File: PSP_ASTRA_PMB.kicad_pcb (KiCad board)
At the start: 2 copper layers, 15 parts, among them J1 Conn_01x02_Socket, J2 Conn_01x01_Socket, J3 Screw_Terminal_01x03, J5 Screw_Terminal_01x01, J6 Screw_Terminal_01x01, Q1 BSC014N04LSIATMA1, U1 INA226, U5 LD1117V33

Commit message: Add files via upload
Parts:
- moved J6 42.8 mm to (151.0, 110.0)
- moved J5 33.3 mm to (150.0, 84.5)
- moved U5 23.6 mm to (145.4, 93.5)
- moved C3 18.4 mm to (154.0, 97.5), turned to 180 degrees
- moved R2 18.3 mm to (143.5, 105.0)
- moved C2 15.5 mm to (148.5, 97.5)
- moved C1 15.5 mm to (143.5, 98.0), turned to 180 degrees
- moved J1 14.7 mm to (138.5, 101.4), turned to -90 degrees
- moved Q1 13.2 mm to (170.5, 110.0)
- moved R3 11.9 mm to (143.5, 101.5)
- moved J3 9.50 mm to (133.0, 94.0), turned to 90 degrees
- moved R4 5.03 mm to (165.0, 89.0)
- moved J2 3.16 mm to (156.0, 103.5)
- moved U1 2.06 mm to (150.5, 102.0)
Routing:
- net /Microcontroller: track 0.00 -> 0.85 mm
- added copper zone on B.Cu, net GND
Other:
- copper layers 2 -> 4

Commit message: Add files via upload
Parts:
- Q1: footprint Package_TO_SOT_SMD:TDSON-8-1 -> PSPAC:MOSFETPMB
- R1, R2, R3: footprint Resistor_SMD:R_0805_2012Metric -> Resistor_SMD:R_0805_2012Metric_Pad1.20x1.40mm_HandSolder
- moved R1 21.9 mm to (156.0, 100.5)
- moved Q1 8.49 mm to (162.5, 107.3), turned to -90 degrees
- moved J1 6.08 mm to (144.0, 104.0)
- moved R2 5.25 mm to (143.5, 110.2)
- moved R4 3.15 mm to (168.0, 90.0)
- moved C3 1.00 mm to (155.0, 97.5)
- moved J2 0.71 mm to (155.5, 104.0)
- moved U1 0.50 mm to (150.0, 102.0)
- moved U5 0.30 mm to (145.5, 93.2)
- moved J6 0.25 mm to (150.8, 110.0)
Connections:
- net Net-(Q1-D) renamed /Drain
- J6 pad 1: Net-(J6-Pin_1) -> /Source
- Q1 pad 4: (no net) -> /Microcontroller
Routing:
- net +12V: track 0.00 -> 33.7 mm, vias 0 -> 7
- net Net-(U1-VS): track 0.00 -> 32.0 mm
- net GND: track 0.00 -> 11.8 mm, vias 0 -> 6
- net /Drain: track 0.00 -> 11.4 mm, vias 0 -> 7
- net Net-(J1-Pin_2): track 0.00 -> 10.9 mm
- net /Microcontroller: track 0.85 -> 8.91 mm
- net Net-(J1-Pin_1): track 0.00 -> 6.84 mm
- net /Source: vias 0 -> 6
- added copper zone on B.Cu, net +12V
- added copper zone on F.Cu, net +12V
- added copper zone on In1.Cu, net +12V
- added copper zone on In2.Cu, net +12V
- added copper zone on B.Cu, net /Drain
- added copper zone on F.Cu, net /Drain
- added copper zone on In1.Cu, net /Drain
- added copper zone on In2.Cu, net /Drain
- added copper zone on B.Cu, net /Source
- added copper zone on F.Cu, net /Source
- added copper zone on In1.Cu, net /Source
- added copper zone on In2.Cu, net /Source
- added copper zone on In1.Cu, net GND
- removed copper zone on B.Cu, net GND
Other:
- board outline added: 47 x 36 mm

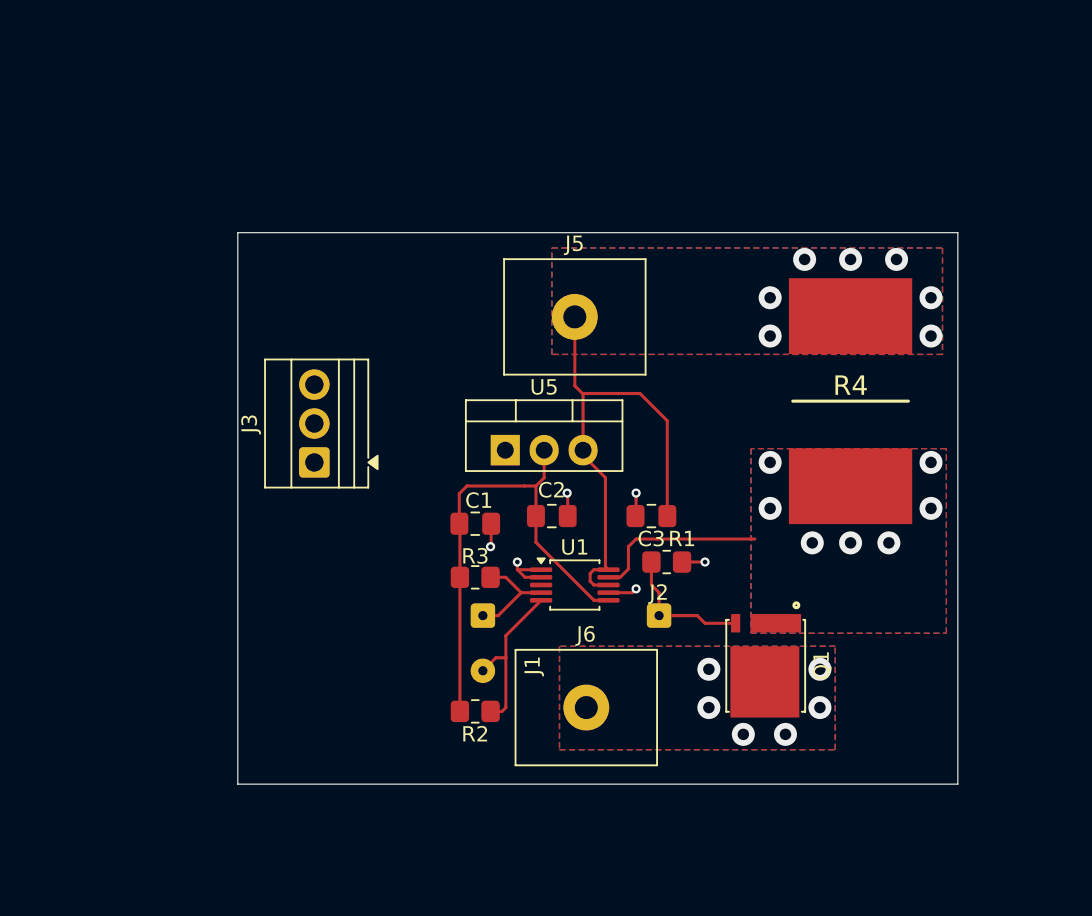
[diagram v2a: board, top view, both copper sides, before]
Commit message: Add files via upload
added pmos and voltage divider (see schematic)
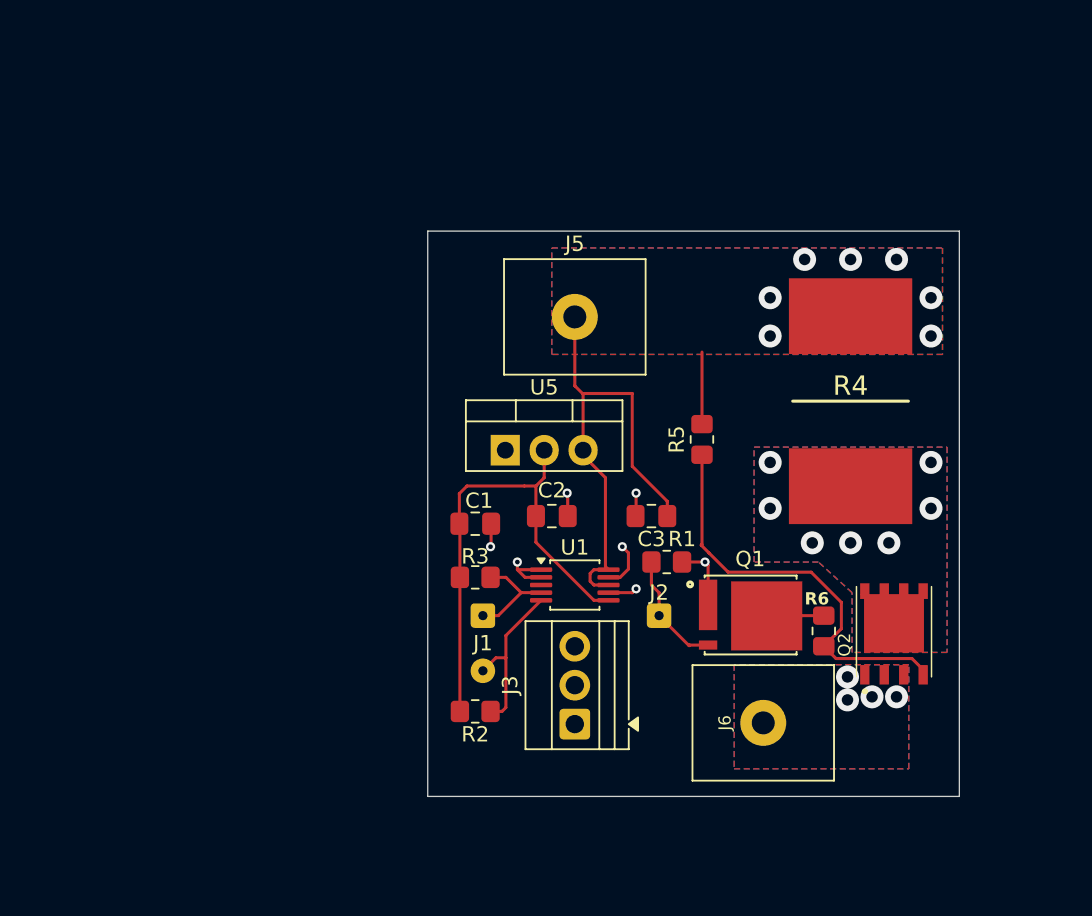
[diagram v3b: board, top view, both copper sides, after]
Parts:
- added Q2: PMOS, PSPAC:PMOSPMB, F.Cu at (170.8, 105.0)
- added R5: 10k, Resistor_SMD:R_0805_2012Metric_Pad1.20x1.40mm_HandSolder, F.Cu at (158.3, 92.5)
- added R6: 10, Resistor_SMD:R_0805_2012Metric_Pad1.20x1.40mm_HandSolder, F.Cu at (166.2, 105.0)
- moved J3 24.1 mm to (150.0, 111.1)
- moved J6 11.6 mm to (162.3, 111.0)
- moved Q1 3.46 mm to (161.5, 104.0), turned to 0 degrees
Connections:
- J6 pad 1: /Source -> /PMOS Source
- Q1 pad 1: /Drain -> GND
- Q1 pad 8: /Source -> /NMOS Drain
- R4 pad 2: /Drain -> /PMOS Drain
- U1 pad 9: /Drain -> /PMOS Drain
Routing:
- net /PMOS Gate: track 0.00 -> 27.4 mm
- net /PMOS Drain: track 0.00 -> 13.8 mm, vias 0 -> 8
- net /Drain: track 11.4 -> 0.00 mm, vias 7 -> 0
- net /NMOS Drain: track 0.00 -> 4.76 mm
- net +12V: track 33.7 -> 38.2 mm
- net GND: track 11.8 -> 14.6 mm
- net /Microcontroller: track 8.91 -> 7.74 mm
- net /PMOS Source: track 0.00 -> 0.33 mm, vias 0 -> 4
- net /Source: vias 6 -> 0
- added copper zone on B.Cu, net /PMOS Drain
- added copper zone on F.Cu, net /PMOS Drain
- added copper zone on In1.Cu, net /PMOS Drain
- added copper zone on In2.Cu, net /PMOS Drain
- added copper zone on B.Cu, net /PMOS Source
- added copper zone on F.Cu, net /PMOS Source
- added copper zone on In1.Cu, net /PMOS Source
- added copper zone on In2.Cu, net /PMOS Source
- removed copper zone on B.Cu, net /Drain
- removed copper zone on F.Cu, net /Drain
- removed copper zone on In1.Cu, net /Drain
- removed copper zone on In2.Cu, net /Drain
- removed copper zone on B.Cu, net /Source
- removed copper zone on F.Cu, net /Source
- removed copper zone on In1.Cu, net /Source
- removed copper zone on In2.Cu, net /Source
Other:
- board size 47 x 36 mm -> 34.7 x 36.9 mm

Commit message: Add files via upload
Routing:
- net /PMOS Drain: track 13.8 -> 12.1 mm
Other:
- board text added: "${REFERENCE}"
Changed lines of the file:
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@@
 		(tags "THT Terminal Block Xinya XY308-2.54-3P pitch 2.54mm size 8.12x6.5mm drill 1.2mm pad 2mm")
 		(property "Reference" "J3"
-			(at 2.54 -4.22 90)
+			(at -2.47 -0.05 180)
 			(layer "F.SilkS")
 			(effects
@@
 		(tags "capacitor handsolder")
 		(property "Reference" "C3"
-			(at 0 -1.5 0)
+			(at -1.9 1.65 0)
 			(layer "F.SilkS")
 			(effects
@@
 		(at 161.475 103.96)
 		(property "Reference" "Q1"
-			(at -0.02513 -3.65372 0)
+			(at -0.625 -3.56 0)
 			(layer "F.SilkS")
 			(effects
@@
 		(tags "THT single screw terminal block Metz Connect 360271 size 9x7.3mm drill 1.5mm pad 3mm")
 		(property "Reference" "J6"
-			(at -2.5 0 90)
+			(at -2.8 0 0)
 			(layer "F.SilkS")
 			(effects
@@
 			(effects
 				(font
-					(size 1 1)
-					(thickness 0.15)
+					(size 0.8 0.8)
+					(thickness 0.1)
 				)
 			)
@@
 		(tags "THT single screw terminal block Metz Connect 360271 size 9x7.3mm drill 1.5mm pad 3mm")
 		(property "Reference" "J5"
-			(at 0 -4.77 0)
+			(at -2.3 0 90)
 			(layer "F.SilkS")
 			(effects
@@
 		(layer "Edge.Cuts")
 	)
+	(gr_text "${REFERENCE}"
+		(at 166.25 105 90)
+		(layer "F.Fab")
+		(effects
+			(font
+				(size 0.5 0.5)
+				(thickness 0.08)
+			)
+		)
+	)
+	(gr_text "${REFERENCE}"
+		(at 152.15 108.54 90)
+		(layer "F.Fab")
+		(effects
+			(font
+				(size 1 1)
+				(thickness 0.15)
+			)
+		)
+	)
+	(gr_text "${REFERENCE}"
+		(at 162.3 106.23 0)
+		(layer "F.Fab")
+		(effects
+			(font
+				(size 1 1)
+				(thickness 0.15)
+			)
+		)
+	)
 	(segment
 		(start 142.5 101.5)
@@
 	(segment
 		(start 160.75 99)
-		(end 162.75 97)
+		(end 161.8 99)
 		(width 0.2)
 		(layer "In1.Cu")

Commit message: Add files via upload
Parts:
- added H1: MountingHole, MountingHole:MountingHole_3.2mm_M3, F.Cu at (177.0, 77.0)
- added H2: MountingHole, MountingHole:MountingHole_3.2mm_M3, F.Cu at (177.0, 117.0)
- added H3: MountingHole, MountingHole:MountingHole_3.2mm_M3, F.Cu at (140.5, 77.0)
- added H4: MountingHole, MountingHole:MountingHole_3.2mm_M3, F.Cu at (140.5, 117.0)
- C3: value 100n -> 0.1 u
- moved Q2 0.36 mm to (171.2, 105.2), turned to -90 degrees
- turned R6 to 90 degrees
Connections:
- J6 pad 1: /PMOS Source -> /PMOS Drain
- R4 pad 2: /PMOS Drain -> /PMOS Source
- U1 pad 9: /PMOS Drain -> /PMOS Source
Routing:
- net /PMOS Source: track 0.33 -> 13.8 mm, vias 4 -> 8
- net /PMOS Drain: track 12.1 -> 0.33 mm, vias 8 -> 4
- net /PMOS Gate: track 27.4 -> 19.7 mm
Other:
- board size 34.7 x 36.9 mm -> 45.8 x 49.1 mm
- board text removed: "${REFERENCE}"
